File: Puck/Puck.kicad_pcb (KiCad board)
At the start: 2 copper layers, 40 x 56.8 mm, 15 parts, among them J1 TYPE-C-31-M-12, J2 AUTO_PROG_UART, U1 ESP32-C6-MINI-1-H4, U2 MCP9808T-E_MS, U4 AP2112K-3.3TRG1

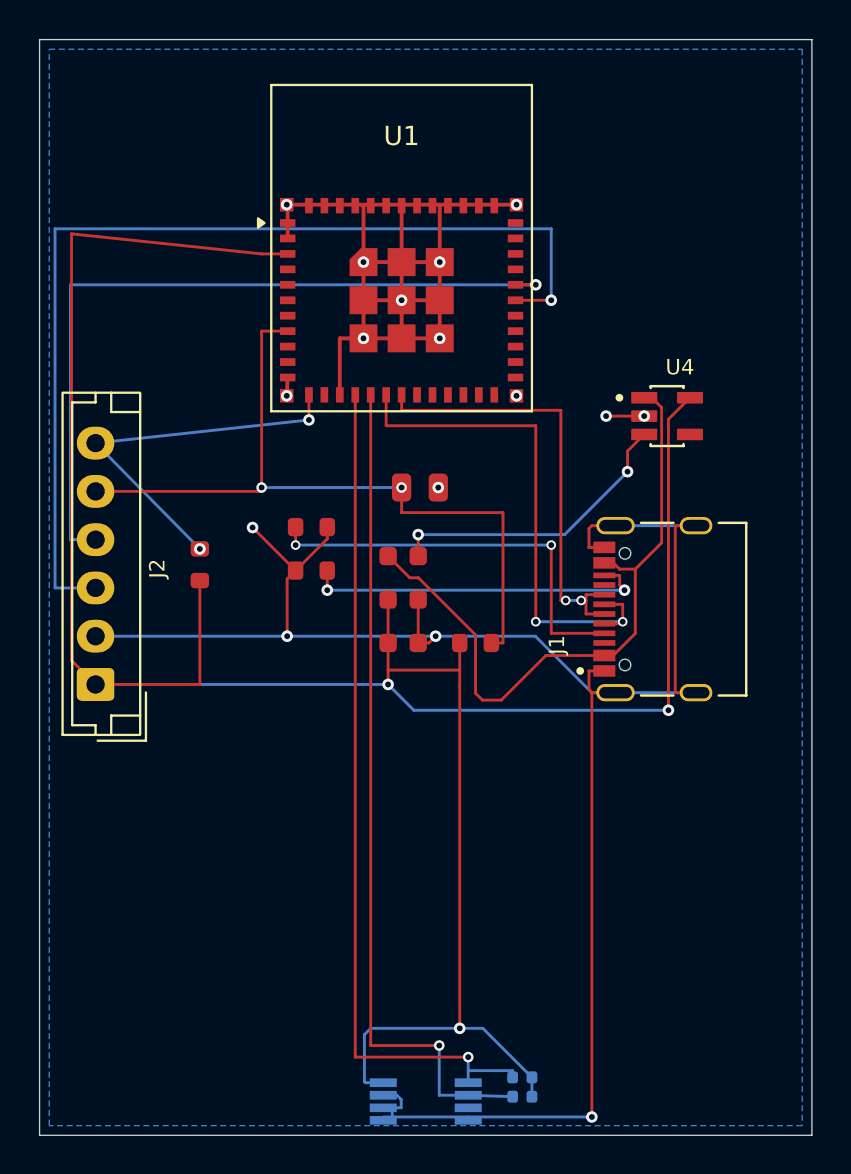
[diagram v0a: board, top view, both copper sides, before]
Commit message: Puck: shrink board 56.8mm→43mm, close sensor dead zone
Move MCP9808T temp sensor (U2) and I2C pull-ups (R1, R2) up 17mm.
Tighten C4/C5/R7 passive cluster. Resize board outline.
FreeRouting v2.2.4 re-routes from scratch; DRC: 0 violations.

Original-author: Zachariah K. Sharma <zachariah.sharma@gmail.com>
Source-commit: 288a401ec4a2f12f302956ca2d00fdc10ee598ae
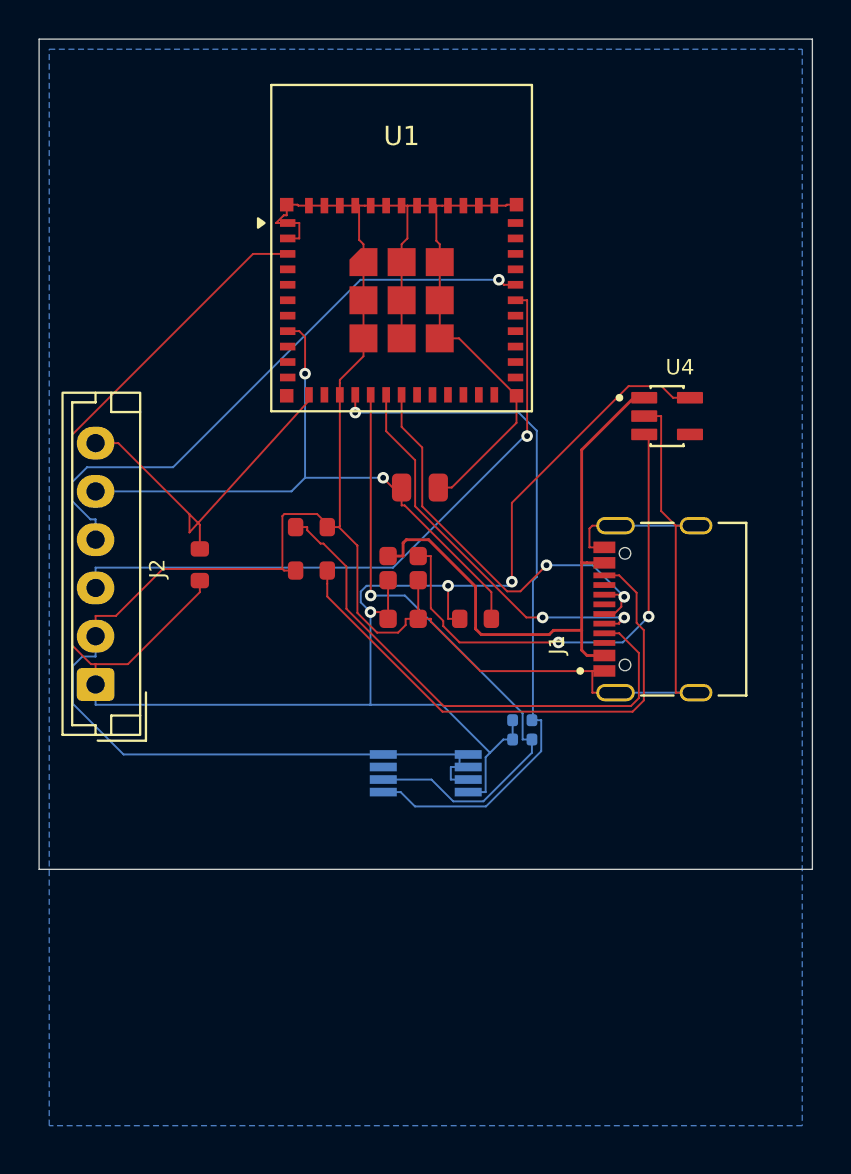
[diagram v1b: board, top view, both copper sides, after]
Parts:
- moved R1 18.5 mm to (149.5, 102.2), turned to 180 degrees
- moved R2 18.5 mm to (149.5, 103.2), turned to 180 degrees
- moved U2 17.0 mm to (144.5, 105.0), turned to 0 degrees
- moved C5 1.25 mm to (143.3, 97.0)
- moved R7 1.25 mm to (147.1, 97.0)
- moved C4 1.00 mm to (143.3, 95.0)
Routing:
- net +3.3V: track 135.1 -> 99.7 mm
- net RXD0: track 52.0 -> 33.9 mm
- net I2C_SCL: track 43.6 -> 32.5 mm
- net Net-(J1-CC2): track 18.1 -> 28.2 mm, vias 2 -> 0
- net Net-(U4-EN): track 15.6 -> 25.6 mm
- net TXD0: track 39.6 -> 31.1 mm
- net I2C_SDA: track 44.1 -> 37.6 mm
- net Net-(J1-CC1): track 21.5 -> 27.7 mm, vias 2 -> 0
- net USB_D-: track 26.9 -> 20.8 mm
- net EN: track 39.4 -> 33.7 mm
- net GND: track 155.5 -> 160.1 mm, vias 16 -> 0
- net VBUS: track 34.2 -> 31.4 mm
- net IO0: track 20.1 -> 18.9 mm, vias 2 -> 0
- net USB_D+: track 23.1 -> 22.4 mm
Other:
- board size 40 x 56.8 mm -> 40.1 x 43 mm

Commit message: Puck: stitch B.Cu GND zone to F.Cu network with 5 vias
The B.Cu GND pour was electrically isolated from the F.Cu GND chain
and from two GND pads on U1 (pins 11 and 52). Added stitching vias
at (140.05, 92.20), (137.35, 84.50), (137.30, 85.45), (141.275, 80.50)
and (143.250, 80.50) to bridge the zones into one GND net.

DRC now reports 0 violations and 1 remaining unconnected item:
USB_D- A7 <-> B7 on J1. That tie cannot be routed under the board's
0.5mm via / 0.15mm clearance / 0.25mm hole clearance rules without a
DRU exception or a manual GUI re-route -- documented in BUILD_NOTES.

Original-author: Zachariah K. Sharma <zachariah.sharma@gmail.com>
Source-commit: 7a85acbdcae1d01382658960f414c670ec81e087
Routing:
- net GND: vias 0 -> 5
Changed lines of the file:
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@@
+		(net 2)
+	)
+	(via
+		(at 140.05 92.2)
+		(size 0.6)
+		(drill 0.3)
+		(layers "F.Cu" "B.Cu")
+		(net 2)
+	)
+	(via
+		(at 143.25 80.5)
+		(size 0.6)
+		(drill 0.3)
+		(layers "F.Cu" "B.Cu")
+		(net 2)
+	)
+	(via
+		(at 137.3 85.45)
+		(size 0.6)
+		(drill 0.3)
+		(layers "F.Cu" "B.Cu")
+		(net 2)
+	)
+	(via
+		(at 137.35 84.5)
+		(size 0.6)
+		(drill 0.3)
+		(layers "F.Cu" "B.Cu")
+		(net 2)
+	)
+	(via
+		(at 141.275 80.5)
+		(size 0.6)
+		(drill 0.3)
+		(layers "F.Cu" "B.Cu")
 		(net 2)
 	)

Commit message: Optimized the sizes of the PCB's
Original-author: Zachariah K. Sharma <zachariah.sharma@gmail.com>
Source-commit: 3995d452baa3285db122d869f4c873083a9268d3
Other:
- board size 40.1 x 43 mm -> 40.1 x 40.6 mm
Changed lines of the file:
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@@
 		(model "${KIPRJMOD}/Comps/Models/ESP32-C6-MINI-1.STEP"
 			(offset
-				(xyz 0 0 0)
+				(xyz -6.5 -5.5 0)
 			)
 			(scale
@@
 			)
 			(rotate
-				(xyz 0 0 0)
+				(xyz -0 -0 -0)
 			)
 		)
@@
 	(gr_rect
 		(start 124.475 66.975)
-		(end 164.525 109.975)
+		(end 164.525 107.575)
 		(stroke
 			(width 0.05)

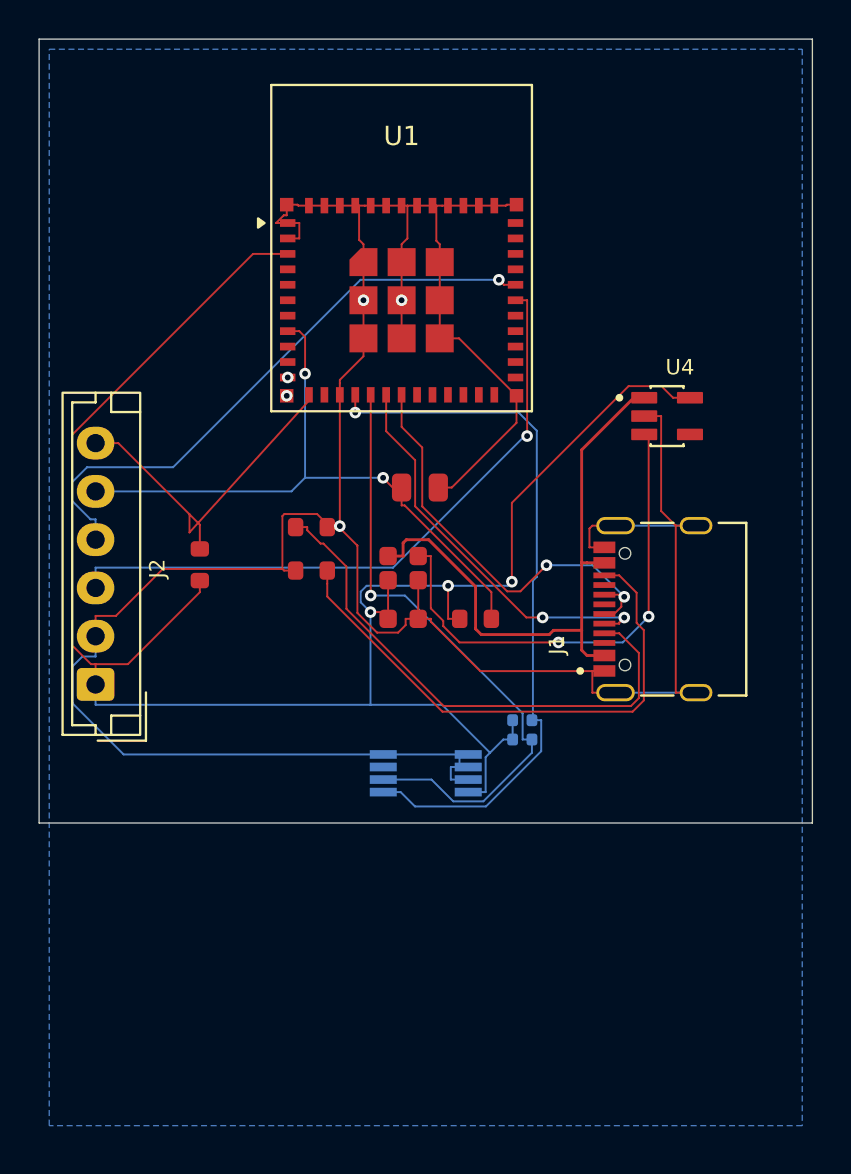
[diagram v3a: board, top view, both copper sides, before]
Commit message: Puck: convert to single-sided assembly (R1/R2/U2 -> F.Cu)
Flip R1, R2, U2 from B.Cu to F.Cu so all 15 components populate one side
(single reflow pass); board stays 2-layer copper. Re-route the sensor
pocket: GND links + via to B.Cu pour, I2C escapes to trunks, and +3.3V's
U2 leg on B.Cu (bottom F.Cu channel too narrow under the SDA via per the
0.5mm edge clearance). DRC: 0 violations, 1 documented USB_D- unconnected.

Original-author: Zachariah K. Sharma <zachariah.sharma@gmail.com>
Source-commit: d1cadbb81f829475b03b8dcef1e482e136ce2b5f
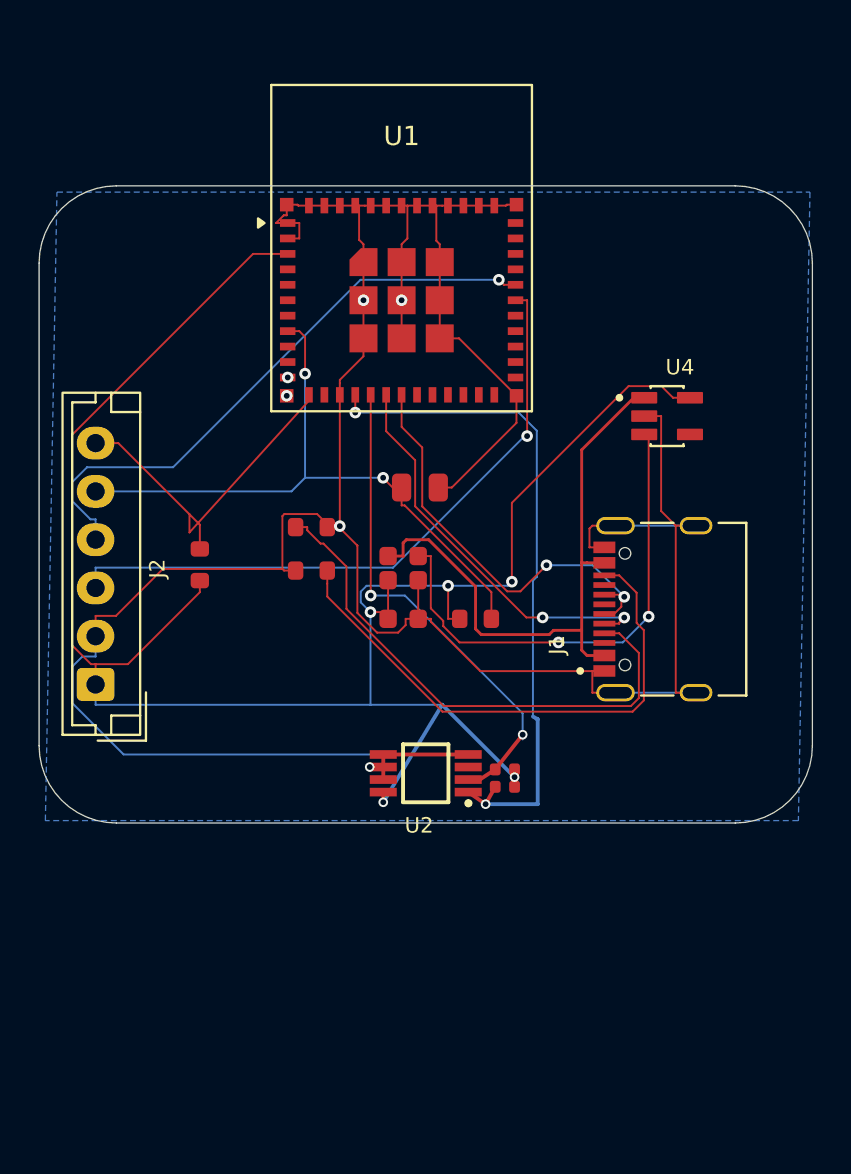
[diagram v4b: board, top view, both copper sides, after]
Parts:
- R1, R2, U2: moved to F.Cu
- moved R1 3.57 mm to (148.6, 105.7), turned to 0 degrees
- moved R2 1.79 mm to (148.6, 104.8), turned to 0 degrees
- turned U2 to 180 degrees
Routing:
- net +3.3V: track 99.7 -> 106.7 mm, vias 3 -> 5
- net I2C_SCL: track 32.5 -> 26.0 mm, vias 1 -> 2
- net I2C_SDA: track 37.6 -> 35.4 mm, vias 1 -> 2
- net GND: track 160.1 -> 158.9 mm, vias 5 -> 6
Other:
- board size 40.1 x 40.6 mm -> 40.1 x 33 mm
